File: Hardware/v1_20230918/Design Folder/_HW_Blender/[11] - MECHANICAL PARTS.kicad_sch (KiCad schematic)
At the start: 9 parts

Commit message: Updating Library
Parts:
- C1101: symbol _SCHLIB_Blender:CAP_1nF_500V_X7R_C0805 -> _SCHLIB_Blender:CAP_CER_1nF_500V_X7R_C0805
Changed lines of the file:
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@@
     )
   )
-  (symbol (lib_id "_SCHLIB_Blender:CAP_1nF_500V_X7R_C0805") (at 172.72 144.78 270) (unit 1)
+  (symbol (lib_id "_SCHLIB_Blender:CAP_CER_1nF_500V_X7R_C0805") (at 172.72 144.78 270) (unit 1)
     (in_bom yes) (on_board yes) (dnp no)
     (property "Reference" "C1101" (at 175.26 146.05 90)

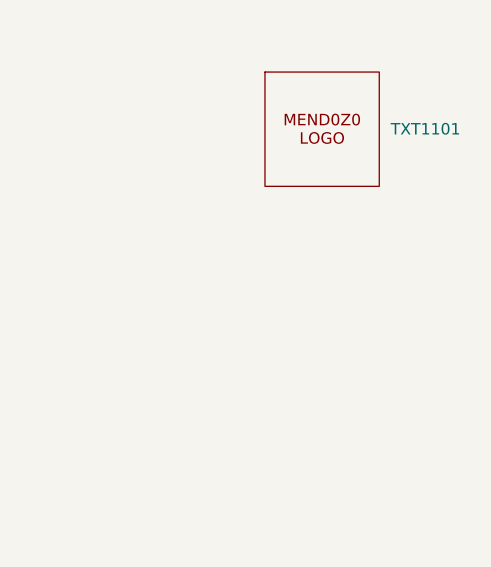
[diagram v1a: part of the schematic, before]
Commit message: Updating 3D components
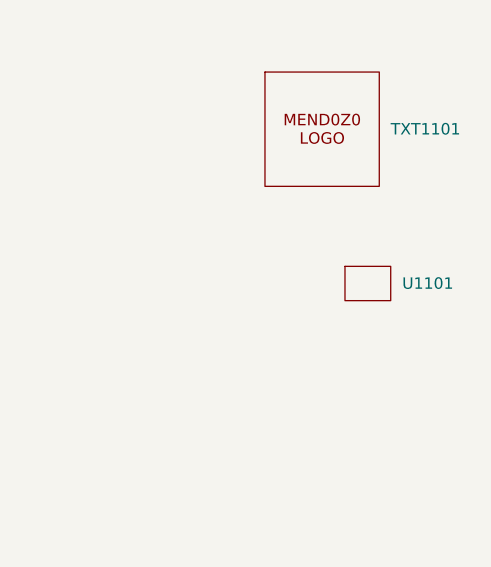
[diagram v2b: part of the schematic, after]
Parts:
- added U1101: ~, _PCBLIB_Blender:OLED, symbol _SCHLIB_Blender:OLED
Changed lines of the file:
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@@
+    )
+  )
+  (symbol (lib_id "_SCHLIB_Blender:OLED") (at 236.22 124.46 0) (unit 1)
+    (in_bom yes) (on_board yes) (dnp no) (fields_autoplaced)
+    (property "Reference" "U1101" (at 242.57 126.365 0)
+      (effects (font (size 1.27 1.27)) (justify left))
+    )
+    (property "Value" "~" (at 236.22 124.46 0)
+      (effects (font (size 1.27 1.27)))
+    )
+    (property "Footprint" "_PCBLIB_Blender:OLED" (at 248.92 118.11 0)
+      (effects (font (size 1.27 1.27)) hide)
+    )
+    (property "Datasheet" "" (at 236.22 124.46 0)
+      (effects (font (size 1.27 1.27)) hide)
+    )
+    (instances
+      (project "_HW_Blender"
+        (path "/6c932160-8052-463b-a5c6-81033be85928/1f48330e-812d-437c-bfc0-24824ee897ea"
+          (reference "U1101") (unit 1)
+        )
+      )
     )
   )
